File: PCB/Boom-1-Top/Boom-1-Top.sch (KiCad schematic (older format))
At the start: 1002 parts, among them J1 DEBUG, J10 PIC_DEBUG, J11 PIC_DEBUG, J12 PIC_DEBUG, J13 PIC_DEBUG, J14 PIC_DEBUG, J15 USB_B_Micro, J16 SD_Card, J17 BT_DEBUG, J18 12V Supply, J19 3V3 Bypass, J2 MIDI IN, J20 5V Bypass, J21 Env +12V Supply, J22 Env -12V Supply, J23 OLEDConn, J24 FiltConn1PassThru, J25 LeftI2C0Test, J26 AudioOutConn, J27 FiltConn2PassThru, J28 FiltConn2PassThruPower, J29 LeftI2C1Test, J3 MIDI OUT, J30 LeftI2C2Test, J31 LeftI2C3Test, J32 RightI2C0Test, J33 RightI2C1Test, J34 RightI2C2Test, J35 RightI2C3Test, J36 SPIBus1Test, J37 Osc1Conn, J38 Osc2Conn, J39 SubNoiseConn, J4 PIC_DEBUG, J40 FiltConn2, J41 EnvGenConn2, J42 EnvGenConn1, J43 FXConn1, J44 FiltConn1, J45 FXConn2, J46 EnvGenConn3, J47 BTTestConn, J48 MIDITestConn, J49 I2CBus1TestConn, J5 PIC_DEBUG, J50 I2CBus2TestConn, J51 OLEDTestConn, J52 SDIOTestConn, J6 PIC_DEBUG, J7 PIC_DEBUG, J8 PIC_DEBUG, J9 PIC_DEBUG, Q1 AO3401A, Q2 AO3401A, SW1 Osc1SawEncoder, SW10 SubToOsc2FiltEncoder, SW11 Osc1ToOsc2FiltEncoder, SW12 Osc1FiltFreqEncoder, SW13 Osc2FiltFreqEncoder, SW14 SubFiltFreqEncoder, SW15 OscFiltEnvAttackEncoder, SW16 SubFiltEnvAttackEncoder, SW17 Osc1FiltResEncoder, SW18 Osc2FiltResEncoder, SW19 SubFiltResEncoder, SW2 Osc1SqrEncoder, SW20 OscFiltEnvDecayEncoder, SW21 SubFiltEnvDecayEncoder, SW22 OscFiltEnvSustainEncoder, SW23 SubFiltEnvSustainEncoder, SW24 Osc1DriveEncoder, SW25 Osc2DistortionEncoder, SW26 OscFiltEnvReleaseEncoder, SW27 SubFiltEnvReleaseEncoder, SW28 FXWetDryEncoder, SW29 SubAmpEnvAttackEncoder, SW3 Rotary_Encoder, SW30 OscAmpEnvAttackEncoder, SW31 FXControl1Encoder, SW32 SubAmpEnvDecayEncoder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

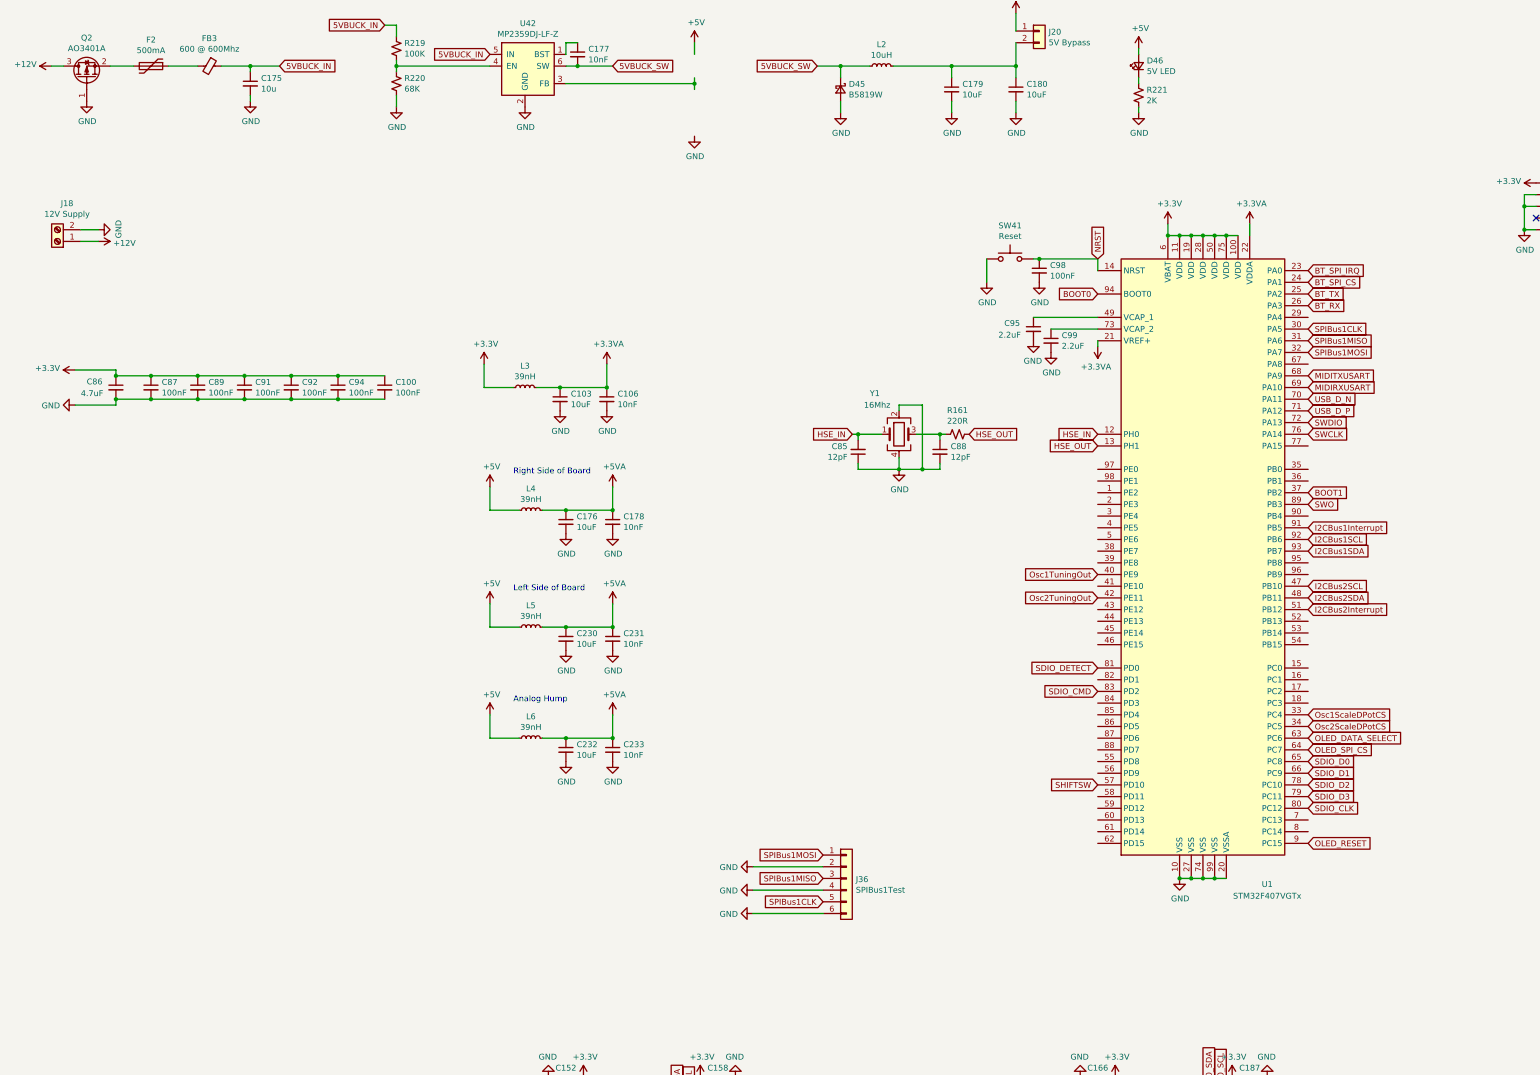
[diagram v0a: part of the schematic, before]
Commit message: schematic for 16v power
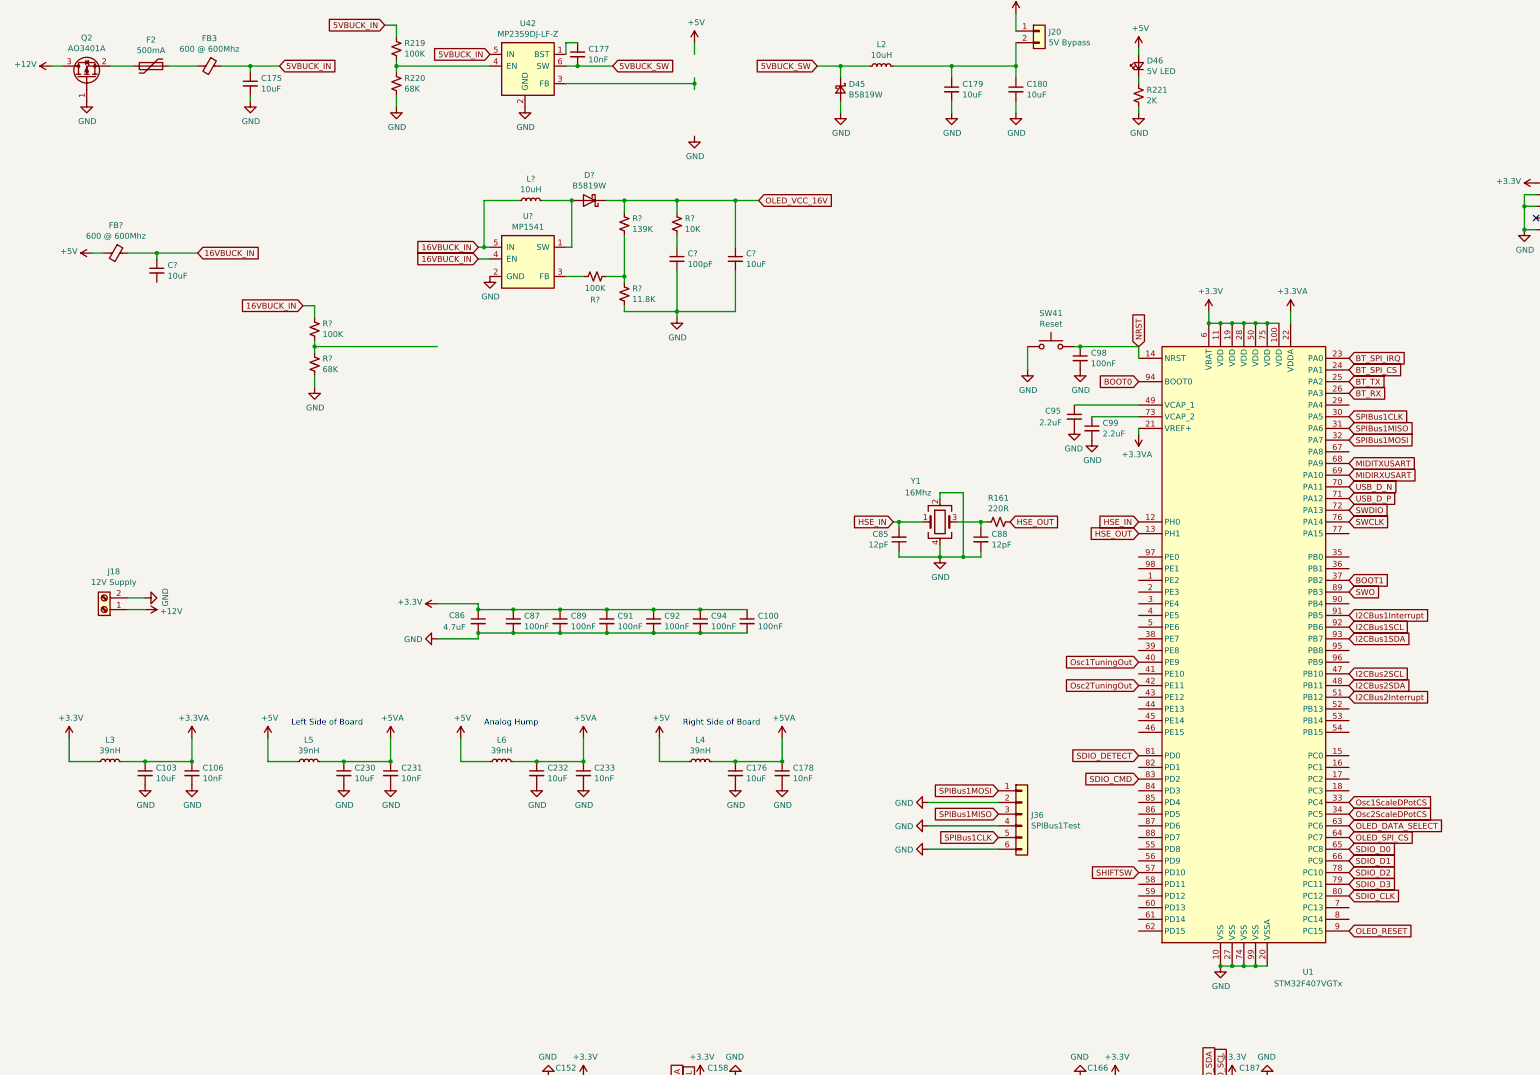
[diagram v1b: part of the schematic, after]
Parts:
- added C? (x2): 10uF, symbol Device:C_Small
- added C?: 100pF, symbol Device:C_Small
- added D?: B5819W, symbol Device:D_Schottky
- added FB?: 600 @ 600Mhz, Inductor_SMD:L_0805_2012Metric, symbol Device:Ferrite_Bead_Small
- added L?: 10uH, Inductor_SMD:L_Sunlord_MWSA0518_5.4x5.2mm, symbol Device:L_Small
- added R?: 100K, Resistor_SMD:R_1206_3216Metric, symbol Device:R_Small_US
- added R?: 68K, Resistor_SMD:R_0603_1608Metric, symbol Device:R_Small_US
- added R?: 139K, symbol Device:R_Small_US
- added R?: 11.8K, symbol Device:R_Small_US
- added R?: 100K, symbol Device:R_Small_US
- added R?: 10K, symbol Device:R_Small_US
- added U?: MP1541, symbol MP1541:MP1541
- C175: value 10u -> 10uF
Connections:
- net +5V: now also FB?.2
- net GND: now also C?.2, C?.2, R?.2, R?.2, U?.2 (GND)
- net OLED_VCC_16V: now also C?.1, D?.1 (K), R?.1, R?.1
- new net: R?.1, R?.2
- new net: D?.2 (A), L?.2, U?.1 (SW)
- new net: R?.1, R?.1, R?.2
- new net: R?.2, U?.3 (FB)
- new net: C?.1, R?.2
- new net 16VBUCK_IN: C?.1, FB?.1, L?.1, R?.1, U?.4 (EN), U?.5 (IN)
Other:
- moved on the sheet: C100, C103, C106, C176, C178, C230, C231, C232, C233, C85, C86, C87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

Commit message: - Added 22R resistors to DEBUG connector - Added BOOT switch
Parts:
- removed R?: 100K, Resistor_SMD:R_1206_3216Metric, symbol Device:R_Small_US
- removed R?: 68K, Resistor_SMD:R_0603_1608Metric, symbol Device:R_Small_US
- added D122: LED, LED_SMD:LED_0603_1608Metric, symbol Device:LED
- added R306: 10K, Resistor_SMD:R_0402_1005Metric, symbol Device:R_Small_US
- added R307, R312, R313, R314: 22R, Resistor_SMD:R_0603_1608Metric, symbol Device:R_Small_US
- added SW63: SW_SPDT, Button_Switch_SMD:SW_SPDT_PCM12, symbol Switch:SW_SPDT
- C234, C235, C236: renamed from C?; footprint (none) -> Capacitor_SMD:C_1206_3216Metric
- D121: renamed from D?; footprint (none) -> Diode_SMD:D_SOD-123
- R163: value 10K -> 1K
- R308, R309, R310, R311: renamed from R?; footprint (none) -> Resistor_SMD:R_1206_3216Metric
- U54: renamed from U?; footprint (none) -> Package_TO_SOT_SMD:TSOT-23-5
- gave numbers to parts that had none: 2
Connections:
- net +3V3: now also SW63.3 (C)
- net BOOT0: now also R306.1; no longer R163.2
- net GND: now also C234.2, R163.2, SW63.1 (A); no longer R163.1
- net NRST: now also R313.1; no longer J1.10 (Pin_10)
- net SWCLK: now also R314.1; no longer J1.4 (Pin_4)
- net SWDIO: now also R307.1; no longer J1.2 (Pin_2)
- net SWO: now also R312.1; no longer J1.6 (Pin_6)
- new net: D122.2 (A), R306.2, SW63.2 (B)
- new net: D122.1 (K), R163.1
- new net: J1.2 (Pin_2), R307.2
- new net: J1.4 (Pin_4), R314.2
- new net: J1.10 (Pin_10), R313.2
- new net: J1.6 (Pin_6), R312.2
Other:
- moved on the sheet: C234, C235, C236, D121, FB2, J1, L7, R164, R308, R309, R310, R311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

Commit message: Added header for haptic engine
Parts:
- added J53: HapticEngine, Connector_PinSocket_2.54mm:PinSocket_1x05_P2.54mm_Vertical, symbol Connector_Generic:Conn_01x05
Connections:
- net +3V3: now also J53.5 (Pin_5)
- net GND: now also J53.1 (Pin_1)
- net LEFT_I2C_0_SCL: now also J53.3 (Pin_3)
- net LEFT_I2C_0_SDA: now also J53.4 (Pin_4)
- net HAPTIC_TRIG: now reaches U1.98 (PE1)
- net HAPTIC_TRIG: now also J53.2 (Pin_2)
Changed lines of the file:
@@
 	10400 5350 10400 5450
 Connection ~ 10400 5450
+$Comp
+L Connector_Generic:Conn_01x05 J53
+U 1 1 609F75AB
+P 22950 14250
+F 0 "J53" H 22868 13825 50  0000 C CNN
+F 1 "HapticEngine" H 22868 13916 50  0000 C CNN
+F 2 "Connector_PinSocket_2.54mm:PinSocket_1x05_P2.54mm_Vertical" H 22950 14250 50  0001 C CNN
+F 3 "~" H 22950 14250 50  0001 C CNN
+	1    22950 14250
+	-1   0    0    1
+$EndComp
+$Comp
+L power:GND #PWR?
+U 1 1 60A98572
+P 23150 14450
+F 0 "#PWR?" H 23150 14200 50  0001 C CNN
+F 1 "GND" H 23155 14277 50  0000 C CNN
+F 2 "" H 23150 14450 50  0001 C CNN
+F 3 "" H 23150 14450 50  0001 C CNN
+	1    23150 14450
+	1    0    0    -1
+$EndComp
+$Comp
+L power:+3.3V #PWR?
+U 1 1 60AA4890
+P 23150 14050
+F 0 "#PWR?" H 23150 13900 50  0001 C CNN
+F 1 "+3.3V" V 23165 14178 50  0000 L CNN
+F 2 "" H 23150 14050 50  0001 C CNN
+F 3 "" H 23150 14050 50  0001 C CNN
+	1    23150 14050
+	0    1    1    0
+$EndComp
+Text GLabel 23150 14350 2    50   Input ~ 0
+HAPTIC_TRIG
+Text GLabel 23150 14250 2    50   Input ~ 0
+LEFT_I2C_0_SCL
+Text GLabel 23150 14150 2    50   Input ~ 0
+LEFT_I2C_0_SDA
+Text GLabel 10400 7350 0    50   Input ~ 0
+HAPTIC_TRIG
 $EndSCHEMATC

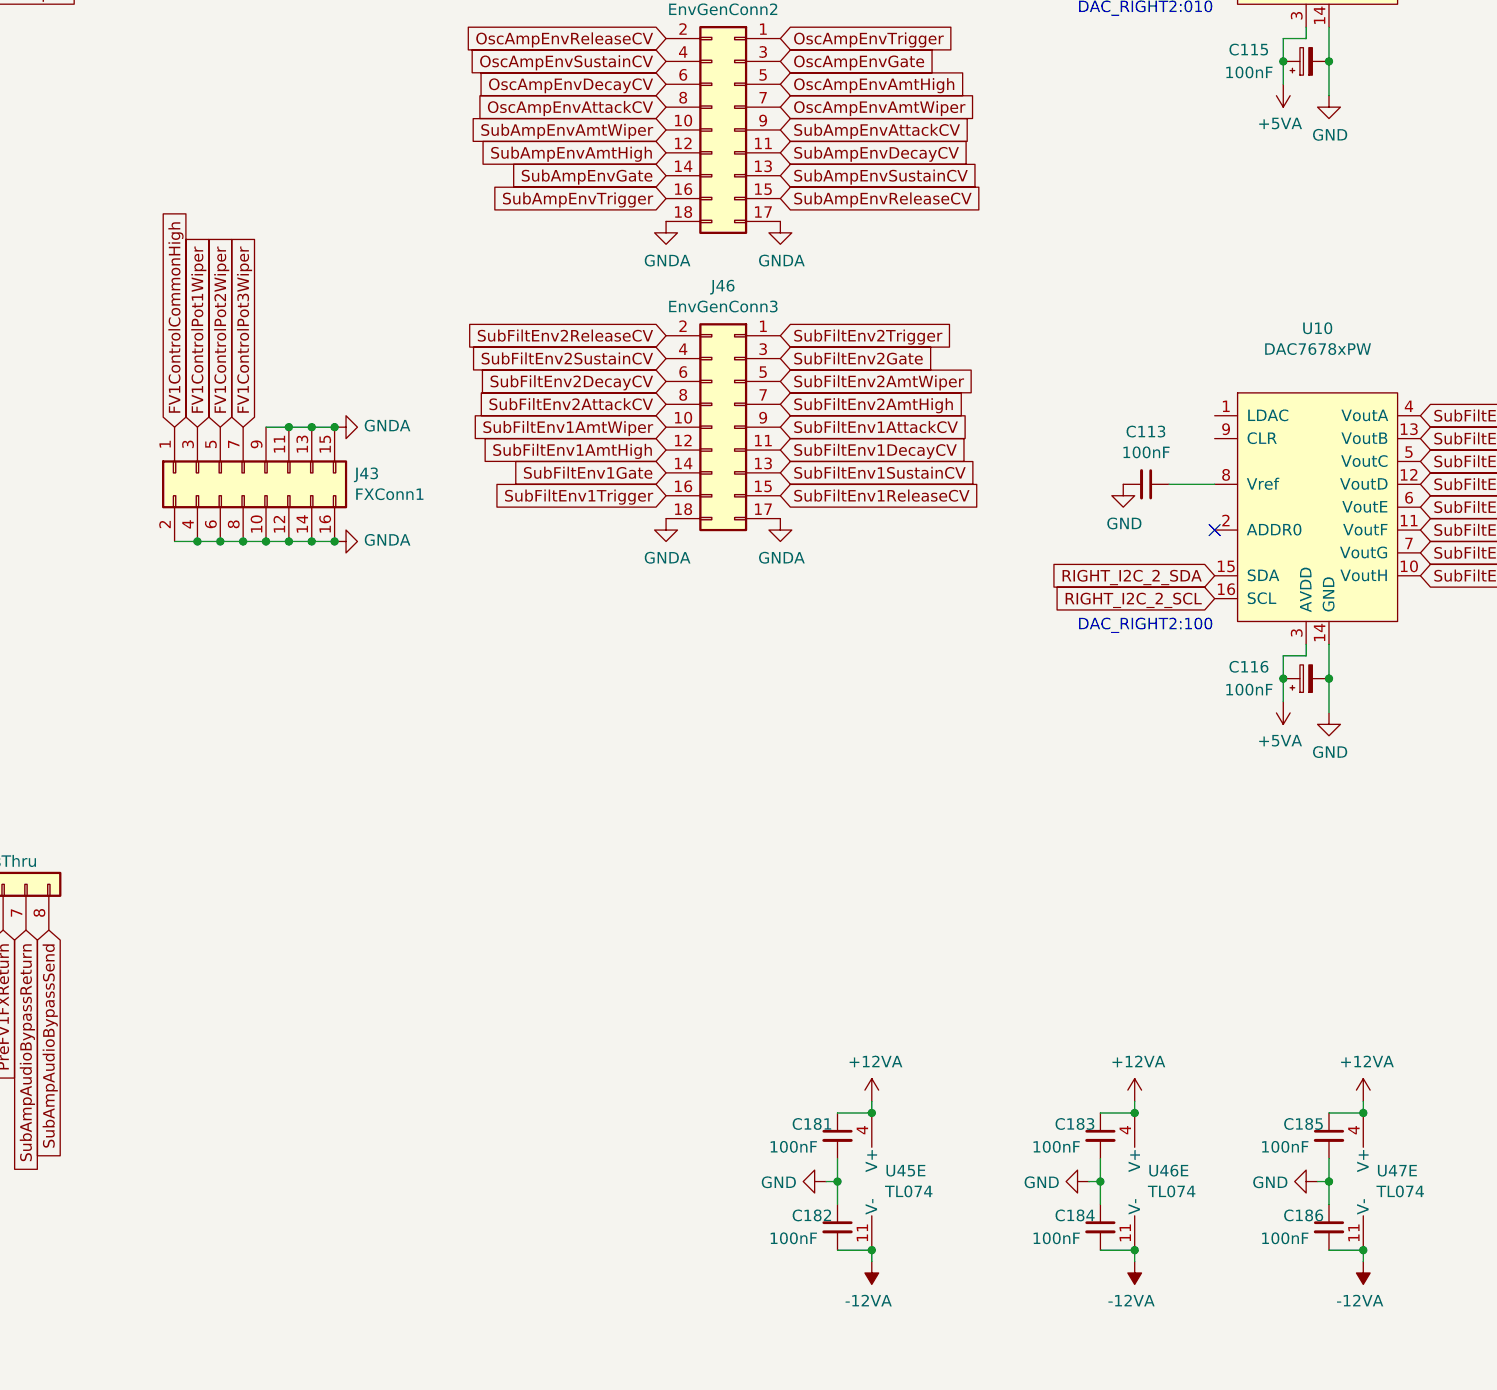
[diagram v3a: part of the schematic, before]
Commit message: Added DPOTs for FV1 control
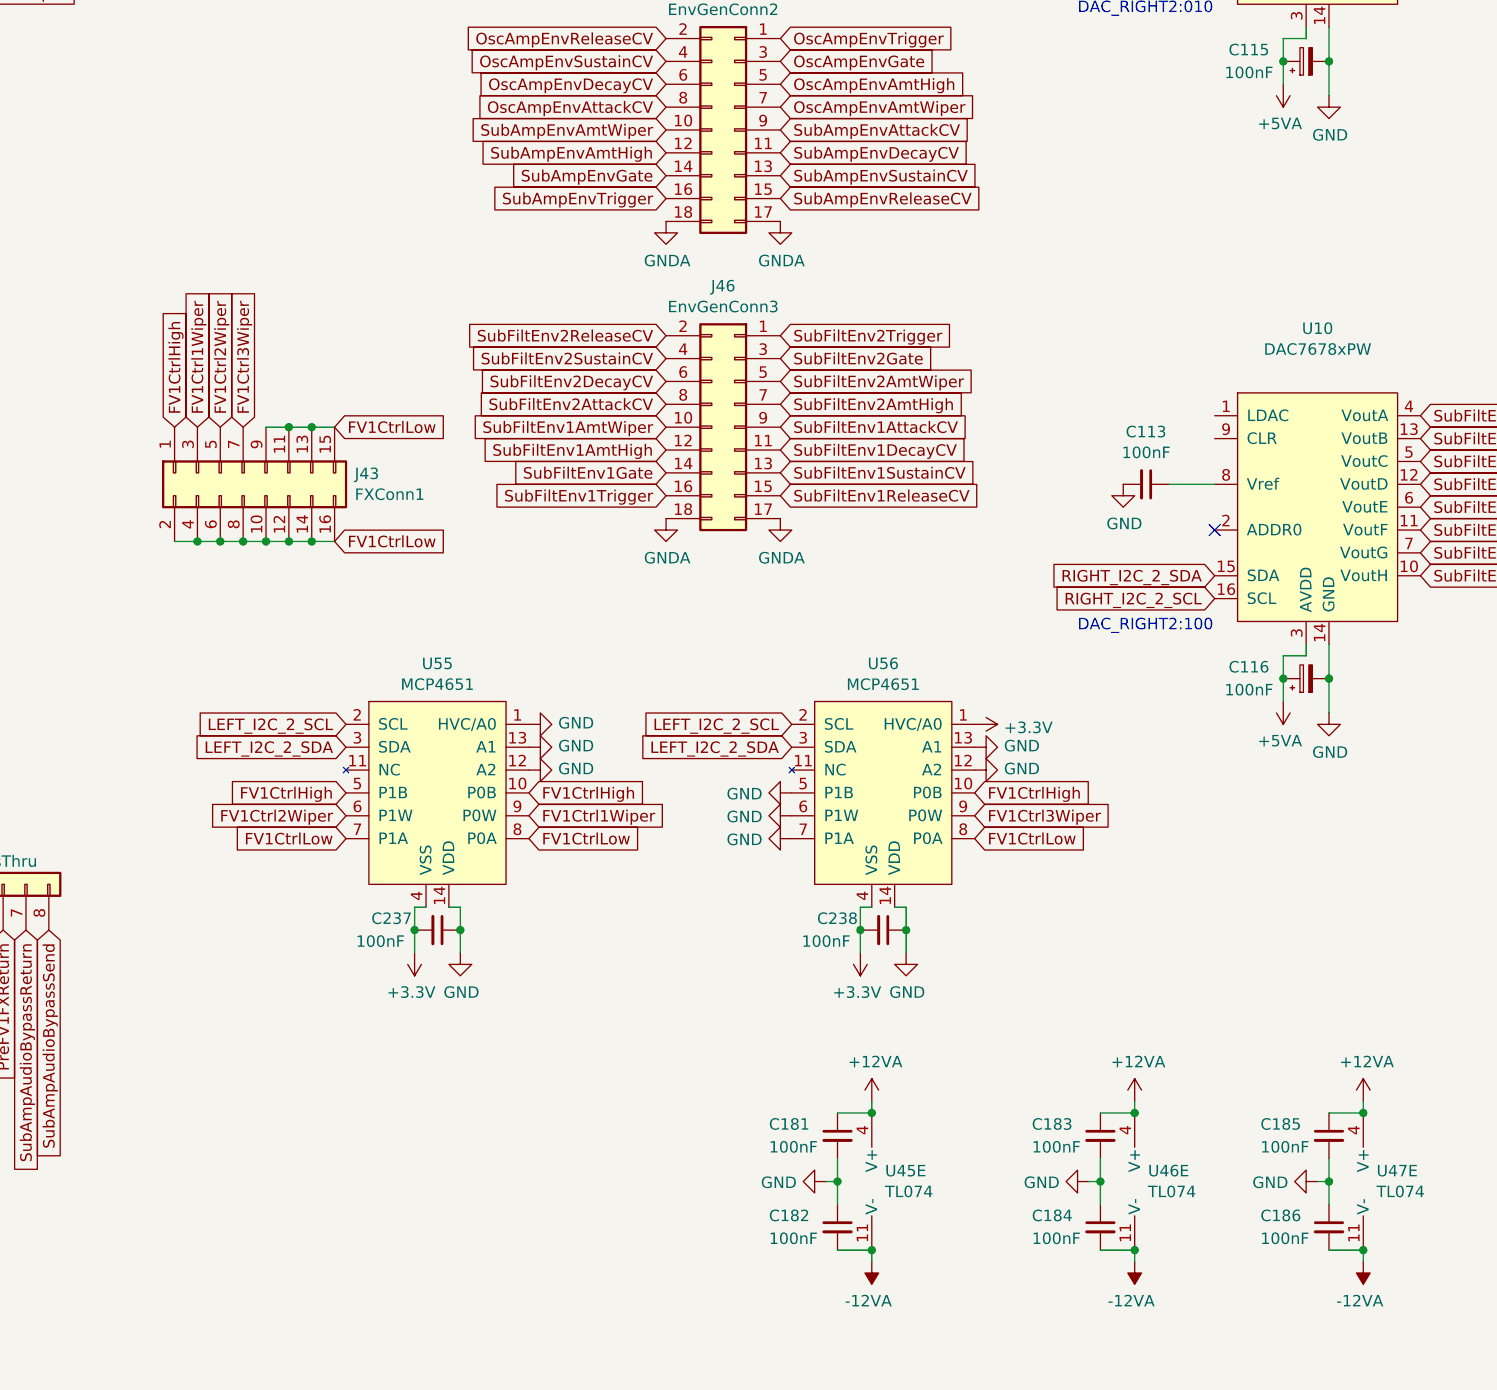
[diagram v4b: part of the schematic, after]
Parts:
- added C237, C238: 100nF, Capacitor_SMD:C_0402_1005Metric, symbol Device:C_Small
- added U55, U56: MCP4651, Package_SO:TSSOP-14_4.4x5mm_P0.65mm, symbol MCP4651:MCP4651
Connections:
- net +3V3: now also C237.2, C238.2, U55.4 (VSS), U56.1 (HVC/A0), U56.4 (VSS)
- net GND: now also C237.1, C238.1, U55.1 (HVC/A0), U55.12 (A2), U55.13 (A1), U55.14 (VDD), U56.12 (A2), U56.13 (A1), U56.14 (VDD), U56.5 (P1B), U56.6 (P1W), U56.7 (P1A)
- net GNDA: no longer J43.10 (Pin_10), J43.11 (Pin_11), J43.12 (Pin_12), J43.13 (Pin_13), J43.14 (Pin_14), J43.15 (Pin_15), J43.16 (Pin_16), J43.2 (Pin_2), J43.4 (Pin_4), J43.6 (Pin_6), J43.8 (Pin_8), J43.9 (Pin_9)
- net LEFT_I2C_2_SCL: now also U55.2 (SCL), U56.2 (SCL)
- net LEFT_I2C_2_SDA: now also U55.3 (SDA), U56.3 (SDA)
- net FV1ControlCommonHigh renamed FV1CtrlHigh
- net FV1CtrlHigh: now also U55.10 (P0B), U55.5 (P1B), U56.10 (P0B)
- net FV1ControlPot1Wiper renamed FV1Ctrl1Wiper
- net FV1Ctrl1Wiper: now also U55.9 (P0W)
- net FV1ControlPot2Wiper renamed FV1Ctrl2Wiper
- net FV1Ctrl2Wiper: now also U55.6 (P1W)
- net FV1ControlPot3Wiper renamed FV1Ctrl3Wiper
- net FV1Ctrl3Wiper: now also U56.9 (P0W)
- new net FV1CtrlLow: J43.10 (Pin_10), J43.11 (Pin_11), J43.12 (Pin_12), J43.13 (Pin_13), J43.14 (Pin_14), J43.15 (Pin_15), J43.16 (Pin_16), J43.2 (Pin_2), J43.4 (Pin_4), J43.6 (Pin_6), J43.8 (Pin_8), J43.9 (Pin_9), U55.7 (P1A), U55.8 (P0A), U56.8 (P0A)
